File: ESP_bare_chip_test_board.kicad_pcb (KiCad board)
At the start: 4 copper layers, 57.1 x 63.5 mm, 92 parts, among them J1101 Conn_01x04, J1201 NorComp - 112-024-113RYY1, J1301 Conn_01x06, J1302 Conn_01x06, J1501 Conn_01x04, J1502 Conn_01x04, J201 Conn_01x06, J501 Barrel_Jack, J502 PWR_IN, J503 ALTERNATE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

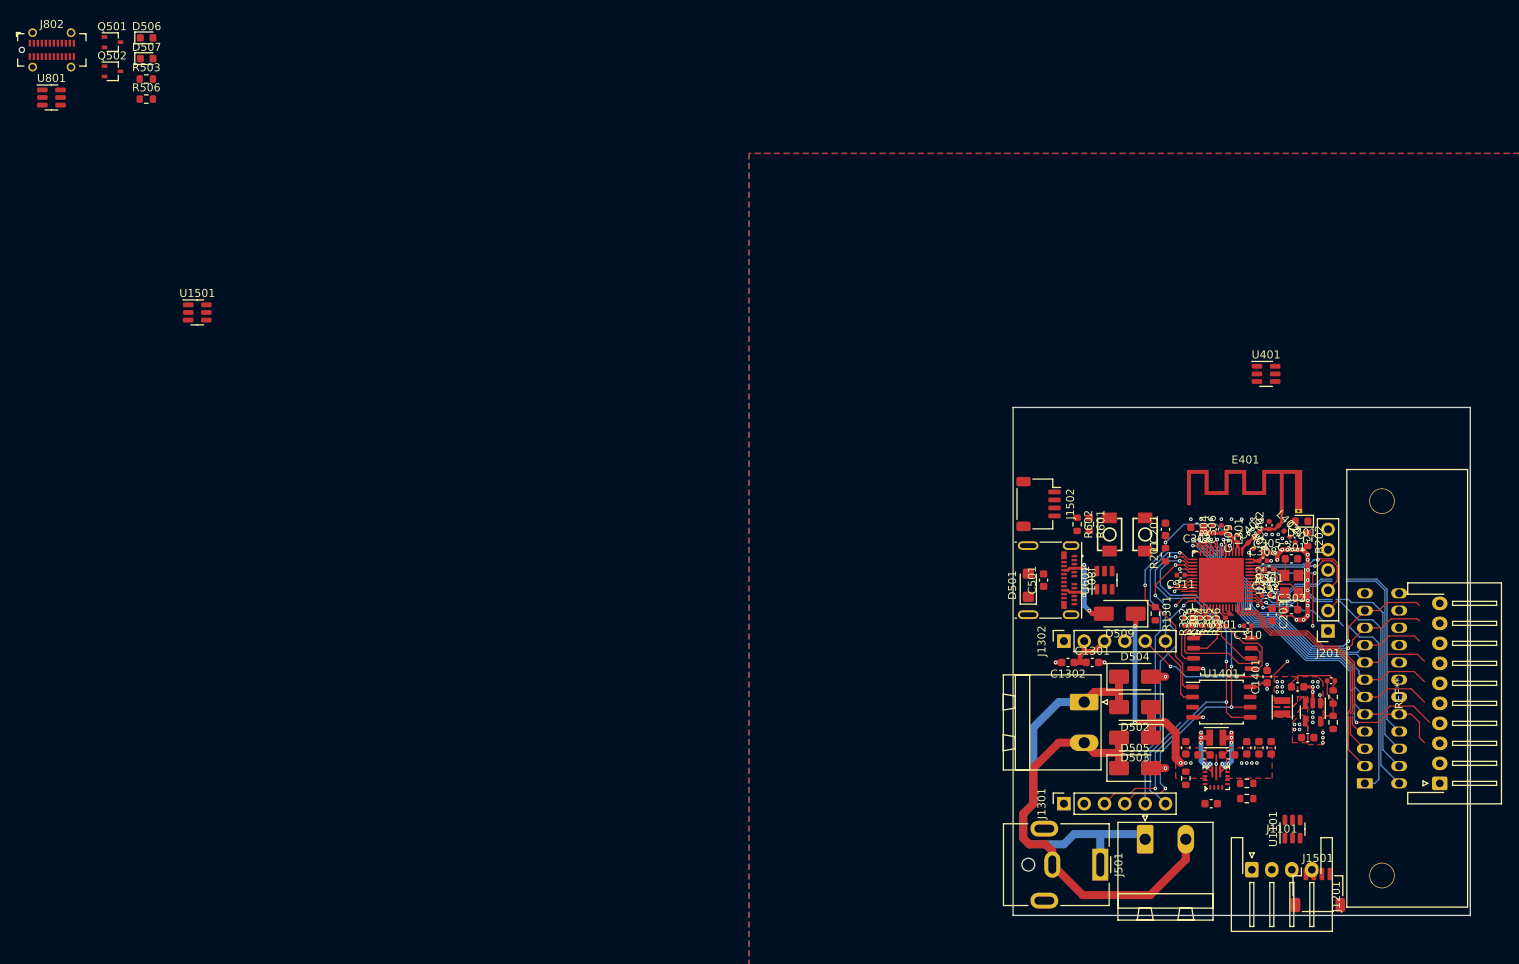
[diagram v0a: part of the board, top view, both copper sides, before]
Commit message: Position final few components
Removed one ESD diode arrray - experimental board, so not really needed,
with the exception of the USB lines.

Add and position 5V indicator LED

Finished wiring up the 5V buck-boost regulator
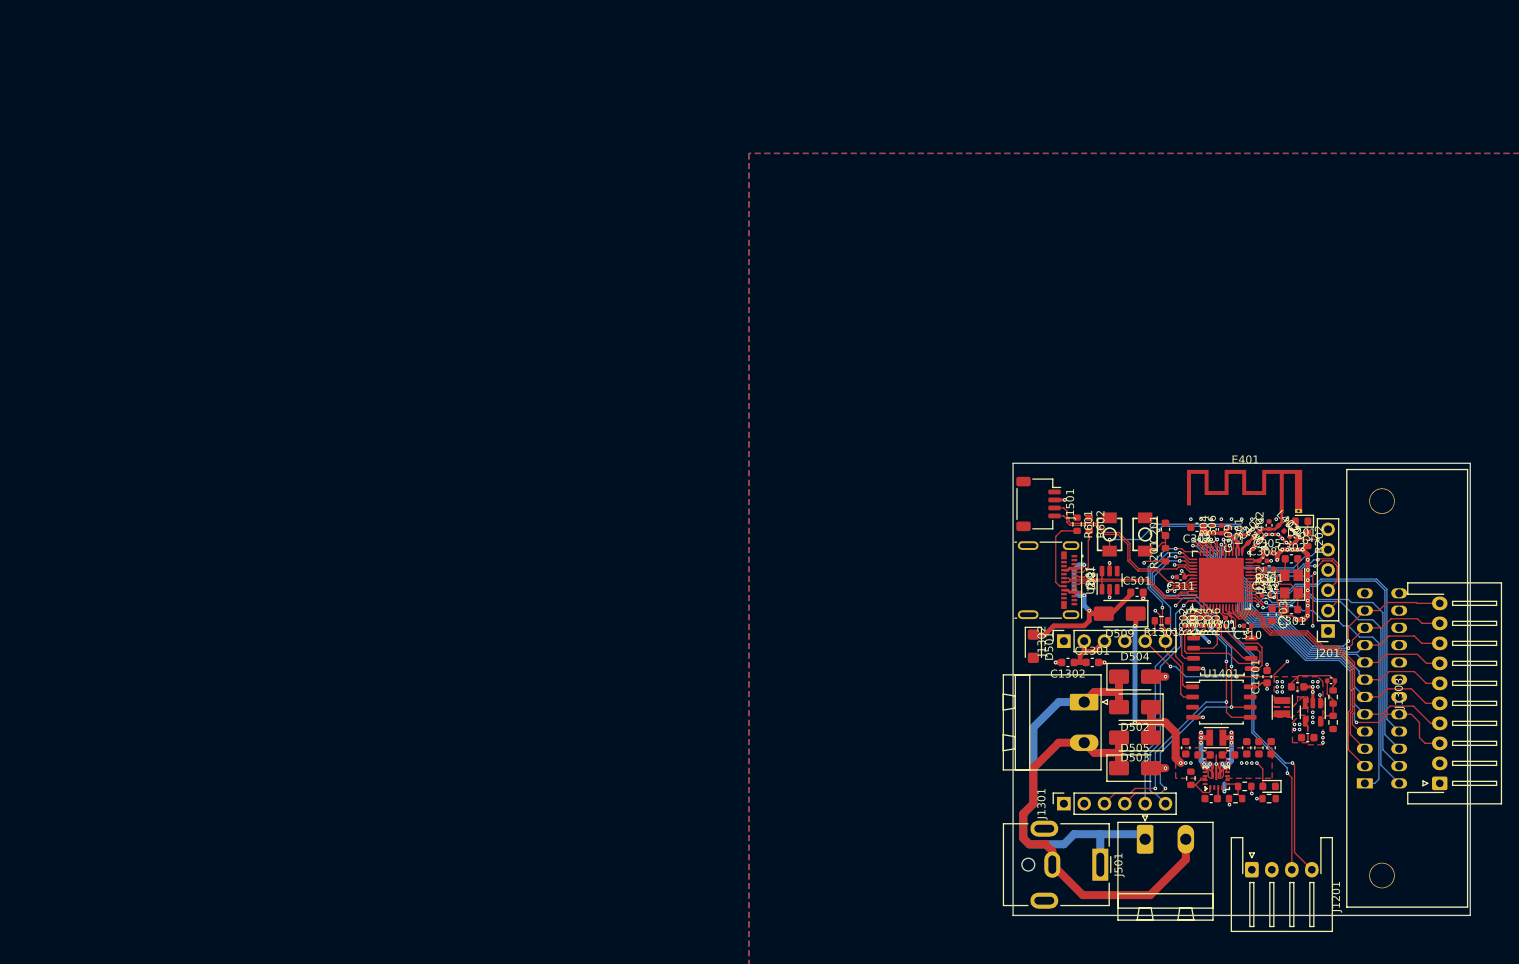
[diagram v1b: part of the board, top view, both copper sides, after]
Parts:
- removed D506: GREEN, LED_SMD:LED_0603_1608Metric
- removed J1502: Conn_01x04, Connector_JST:JST_SH_SM04B-SRSS-TB_1x04-1MP_P1.00mm_Horizontal
- removed J802: USB_C_Receptacle, Connector_USB:USB_C_Receptacle_GCT_USB4115-03-C
- removed Q501, Q502: DTC114E, Package_TO_SOT_SMD:SOT-323_SC-70
- removed R503: 100kΩ, Resistor_SMD:R_0603_1608Metric
- removed REF**: JST_XH_S10B-XH-A-1_1x10_P2.50mm_Horizontal, Connector_JST:JST_XH_S10B-XH-A-1_1x10_P2.50mm_Horizontal
- removed U1101, U1501, U601: D1213A-04TS-7, Package_TO_SOT_SMD:TSOT-23-6
- removed U401: MASWSS0179, Package_TO_SOT_SMD:SOT-23-6
- added J1303: Conn_01x10, Connector_JST:JST_XH_S10B-XH-A-1_1x10_P2.50mm_Horizontal, F.Cu at (167.6, 94.0)
- added NT901: NetTie_2, NetTie:NetTie-2_SMD_Pad0.5mm, B.Cu at (140.7, 94.5)
- moved D507 167.2 mm to (146.3, 94.4), turned to 180 degrees
- moved R506 165.4 mm to (146.3, 95.9), turned to 180 degrees
- moved U801 145.4 mm to (126.4, 68.6), turned to 90 degrees
- moved J1501 59.6 mm to (117.5, 59.1), turned to -90 degrees
- moved C501 11.8 mm to (129.8, 70.1), turned to 0 degrees
- moved D501 7.65 mm to (116.8, 76.8), turned to -90 degrees
- moved C301 6.35 mm to (149.1, 72.3), turned to 180 degrees
- moved C302 6.35 mm to (149.1, 65.9)
- moved R601 1.52 mm to (122.3, 61.6)
- moved R602 1.52 mm to (123.8, 61.6)
- moved R1005 1.40 mm to (142.1, 95.9)
- moved R1301 1.17 mm to (132.8, 73.7), turned to 180 degrees
- moved R1003 0.64 mm to (136.5, 93.3)
- moved C1012 0.63 mm to (139.1, 95.9)
- moved R1004 0.46 mm to (143.3, 94.4)
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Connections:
- J1101 pad 2: Net-(J1101-Pin_2) -> +5V
- J1201 pad 1: /ESP32-S3/IO42 -> /ESP32-S3/IO39
- J1201 pad 13: /ESP32-S3/IO38 -> /ESP32-S3/IO40
- J1201 pad 14: /ESP32-S3/IO37 -> /ESP32-S3/IO38
- J1201 pad 15: /ESP32-S3/IO36 -> /ESP32-S3/IO41
- J1201 pad 16: /ESP32-S3/IO35 -> /ESP32-S3/IO42
- J1201 pad 2: /ESP32-S3/IO41 -> /ESP32-S3/IO35
- J1201 pad 3: /ESP32-S3/IO40 -> /ESP32-S3/IO36
- J1201 pad 4: /ESP32-S3/IO39 -> /ESP32-S3/IO37
- J1501 pad 2: Net-(J1501-Pin_2) -> +3V3
- J1501 pad 3: /4pin_connector/J0_pin3 -> /ESP32-S3/IO14
- J1501 pad 4: /4pin_connector/J0_pin4 -> /ESP32-S3/IO15
- R506 pad 2: Net-(Q502-C) -> GND
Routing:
- net /4pin_connector/J0_pin4: track 1.29 -> 38.0 mm, vias 0 -> 2
- net /4pin_connector/J0_pin3: track 1.57 -> 36.9 mm, vias 0 -> 2
- net /ESP32-S3/ESP_EN: track 13.6 -> 38.9 mm, vias 2 -> 4
- net /ESP32-S3/IO37: track 50.6 -> 27.2 mm
- net /ESP32-S3/IO40: track 16.4 -> 39.4 mm
- net /ESP32-S3/ESP_BOOT: track 0.89 -> 22.7 mm, vias 1 -> 2
- net GND: track 36.5 -> 58.4 mm, vias 56 -> 71
- net /ESP32-S3/IO39: track 16.4 -> 37.8 mm
- net /USB_D-: track 1.51 -> 22.8 mm, vias 0 -> 2
- net /ESP32-S3/IO14: track 1.93 -> 22.7 mm, vias 1 -> 0
- net /ESP32-S3/IO36: track 50.0 -> 29.2 mm
- net /ESP32-S3/IO15: track 1.90 -> 22.6 mm, vias 1 -> 0
- net /ESP32-S3/IO41: track 18.9 -> 39.4 mm
- net /USB_D+: track 1.39 -> 21.5 mm, vias 0 -> 2
- net /ESP32-S3/IO35: track 48.2 -> 31.5 mm
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- added copper zone on F.Cu, net /Power/buck-boost-5v/L1
- added copper zone on F.Cu, net /Power/buck-boost-5v/L2
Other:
- board size 57.1 x 63.5 mm -> 57.1 x 56.5 mm

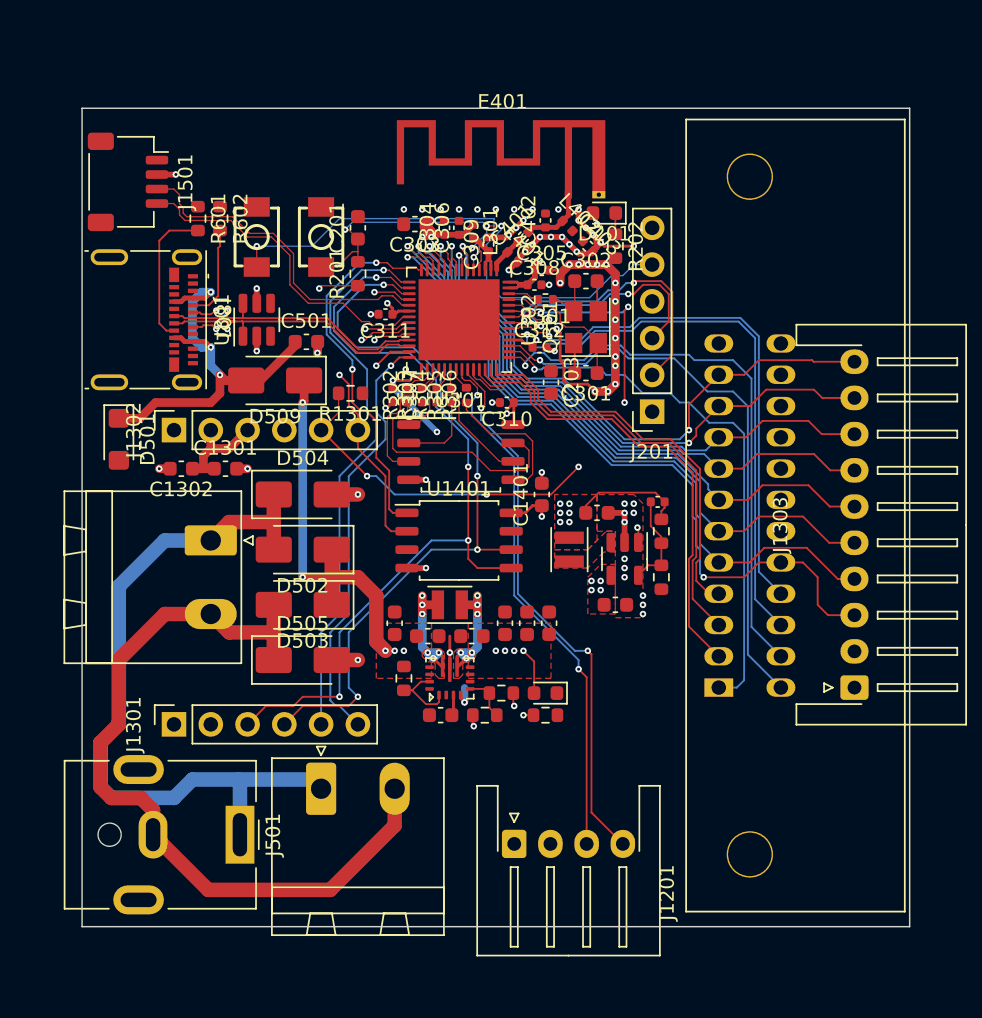
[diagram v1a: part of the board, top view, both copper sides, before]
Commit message: Wire remaining traces, fix DRC errors
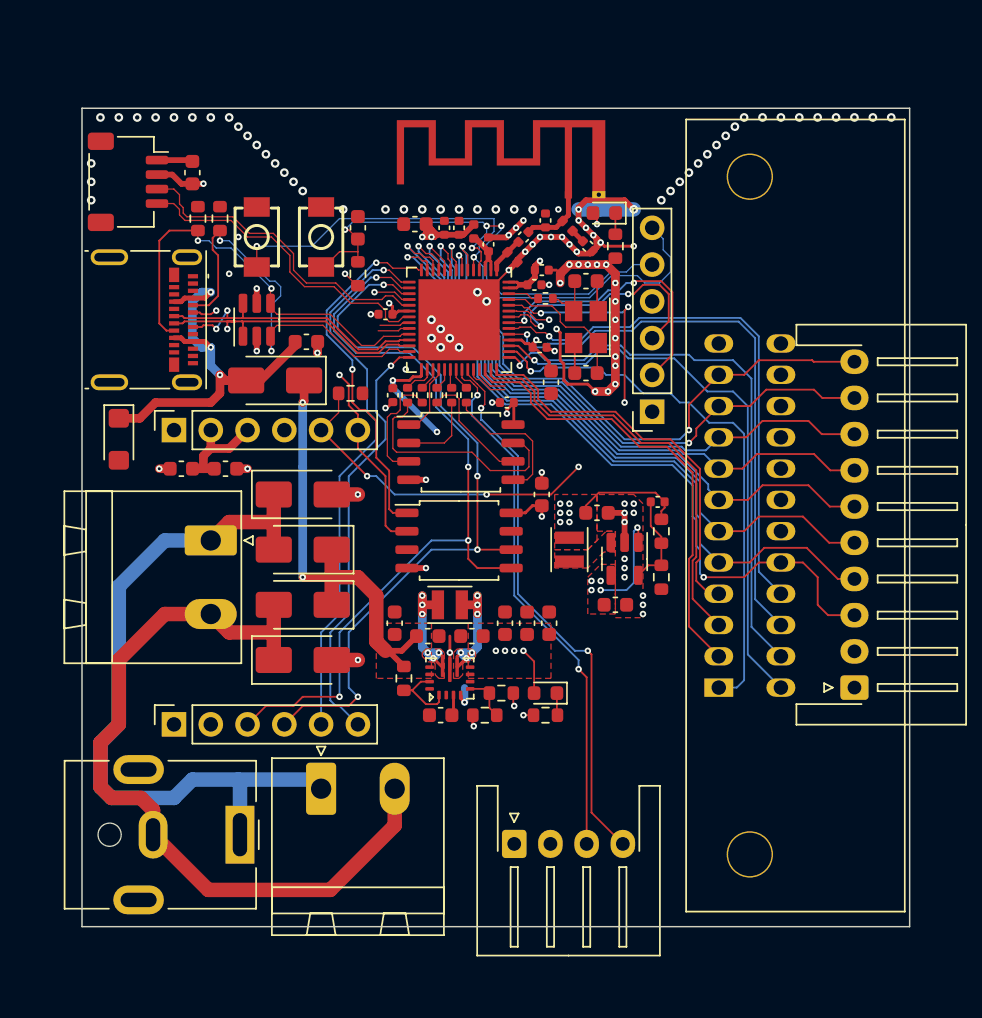
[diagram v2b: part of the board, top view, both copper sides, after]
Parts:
- added C1402: 22uF/6.3V, Capacitor_SMD:C_0603_1608Metric, F.Cu at (121.9, 58.4)
- moved R301 0.08 mm to (146.3, 67.1)
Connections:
- net I2C0.INT renamed /ESP32-S3/IO45
- net I2C0.SCL renamed /ESP32-S3/IO34
- net I2C0.SDA renamed /ESP32-S3/IO33
- U302 pad 24: /ESP32-S3/IO18 -> /USB/CC2
- U302 pad 27: /ESP32-S3/IO21 -> /USB/CC1
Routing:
- net /USB/CC1: track 6.57 -> 30.1 mm, vias 0 -> 2
- net GND: track 58.4 -> 79.0 mm, vias 71 -> 121
- net /ESP32-S3/ESP_BOOT: track 22.7 -> 42.8 mm
- net /USB/CC2: track 9.90 -> 29.4 mm, vias 0 -> 2
- net +5V: track 5.19 -> 11.6 mm
- net /Power/V_{IN}: track 27.1 -> 31.4 mm, vias 5 -> 2
- net +3V3: track 40.2 -> 43.0 mm
- net /ESP32-S3/IO21: track 2.68 -> 0.00 mm, vias 1 -> 0
- net /ESP32-S3/IO18: track 2.57 -> 0.00 mm, vias 1 -> 0
- net (no net): track 2.27 -> 0.00 mm
- net Net-(D507-K): track 0.00 -> 1.54 mm
- net /USB_D+: track 21.5 -> 23.0 mm
- net /ESP32-S3/IO17: track 3.62 -> 2.22 mm, vias 1 -> 0
- net /Power/buck-boost-5v/L2: track 10.4 -> 11.7 mm
- net /Power/buck-boost-5v/L1: track 9.03 -> 10.3 mm
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
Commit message: Add test pads for extra IO pins
Can be soldered to if desired for some testing purpose
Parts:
- added TP101: TestPoint, TestPoint:TestPoint_Pad_D2.0mm, F.Cu at (147.3, 77.5)
- added TP102: TestPoint, TestPoint:TestPoint_Pad_D2.0mm, F.Cu at (151.1, 78.7)
- added TP103: TestPoint, TestPoint:TestPoint_Pad_D2.0mm, F.Cu at (158.1, 66.0)
- added TP104: TestPoint, TestPoint:TestPoint_Pad_D2.0mm, F.Cu at (152.4, 99.1)
- added TP105: TestPoint, TestPoint:TestPoint_Pad_D2.0mm, F.Cu at (146.1, 99.1)
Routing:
- net /ESP32-S3/IO17: track 2.22 -> 70.5 mm, vias 0 -> 4
- net /ESP32-S3/IO16: track 2.10 -> 58.9 mm, vias 0 -> 2
- net /ESP32-S3/IO45: track 3.03 -> 16.2 mm, vias 1 -> 3
- net /ESP32-S3/IO34: track 2.46 -> 12.8 mm
- net /ESP32-S3/IO33: track 3.03 -> 9.64 mm
- net /ESP32-S3/IO41: track 39.4 -> 40.9 mm
- net /ESP32-S3/IO40: track 39.4 -> 40.3 mm
- net GND: vias 121 -> 122

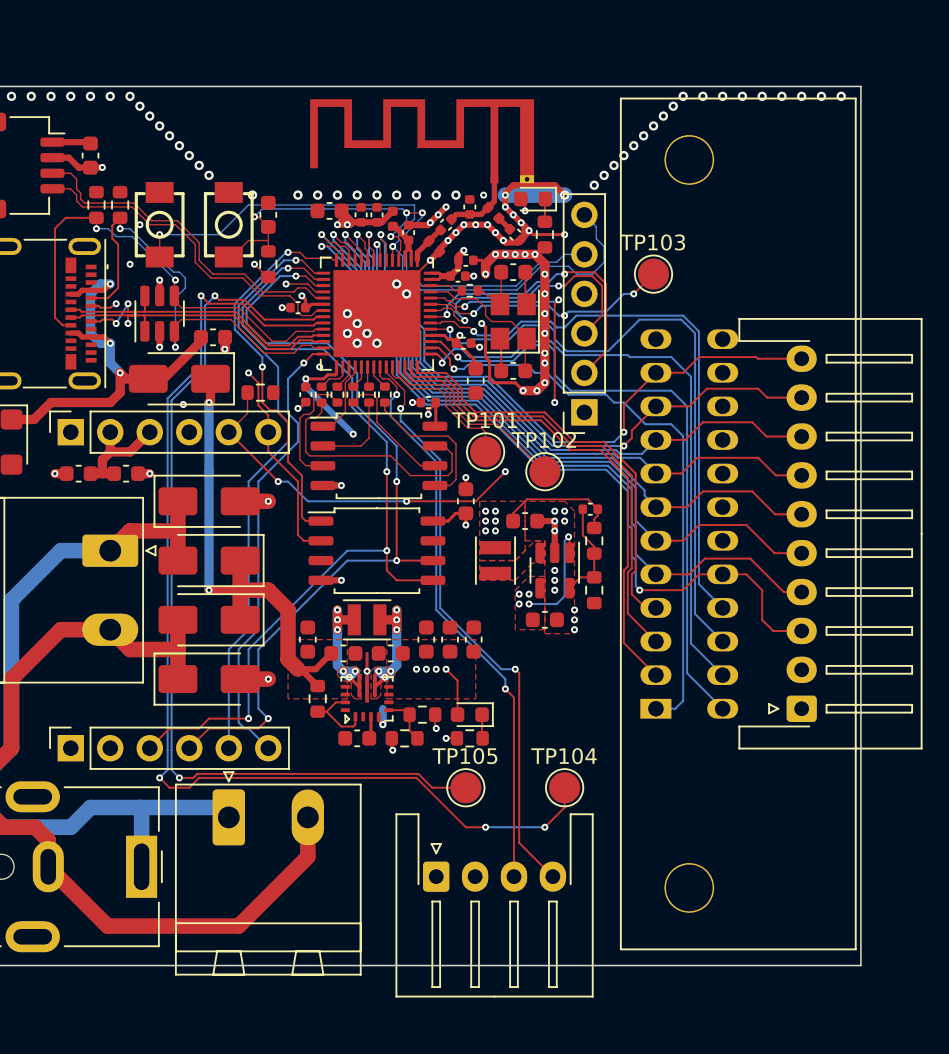
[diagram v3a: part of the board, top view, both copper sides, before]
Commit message: Free up IO26 (to allow for PSRAM)
Had spare IO lines, so may as well use a different one to do ETH_INT
instead of IO26.
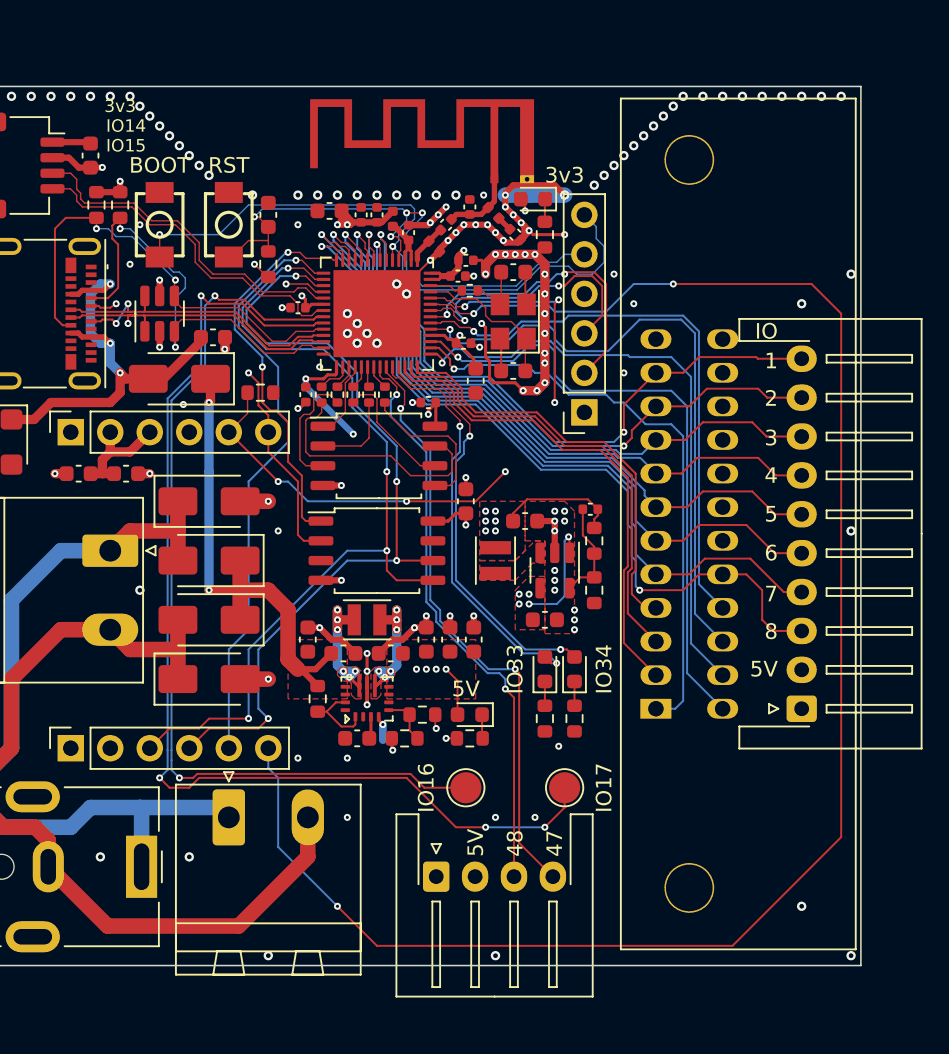
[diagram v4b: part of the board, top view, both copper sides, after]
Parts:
- removed TP101, TP102, TP103: TestPoint, TestPoint:TestPoint_Pad_D2.0mm
- added D101: YELLOW, LED_SMD:LED_0603_1608Metric, F.Cu at (151.1, 91.4)
- added D102: YELLOW, LED_SMD:LED_0603_1608Metric, F.Cu at (153.0, 91.4)
- added R101: 10kΩ, Resistor_SMD:R_0603_1608Metric, F.Cu at (151.1, 94.6)
- added R102: 10kΩ, Resistor_SMD:R_0603_1608Metric, F.Cu at (153.0, 94.6)
- moved NT901 1.00 mm to (140.7, 95.5), turned to -90 degrees
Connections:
- net /4pin_connector/J0_pin3 renamed /IO48
- net /4pin_connector/J0_pin4 renamed /IO47
- U302 pad 28: /~{ETH_INT} -> /ESP32-S3/IO26
- U302 pad 51: /ESP32-S3/IO45 -> /~{ETH_INT}
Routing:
- net /~{ETH_INT}: track 29.5 -> 110.5 mm, vias 1 -> 3
- net /ESP32-S3/IO33: track 9.64 -> 26.8 mm, vias 0 -> 2
- net /ESP32-S3/IO45: track 16.2 -> 0.00 mm, vias 3 -> 0
- net /ESP32-S3/IO34: track 12.8 -> 26.7 mm, vias 0 -> 2
- net GND: track 79.0 -> 91.0 mm, vias 122 -> 151
- net Net-(D102-K): track 0.00 -> 1.56 mm
- net Net-(D101-K): track 0.00 -> 1.56 mm
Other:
- board text added: "1"
- board text added: "2"
- board text added: "3"
- board text added: "3v3"
- board text added: "4"
- board text added: "47"
- board text added: "48"
- board text added: "5"
- board text added: "5V"
- board text added: "6"
- board text added: "7"
- board text added: "8"
- board text added: "BOOT"
- board text added: "IO"
- board text added: "IO14"
- board text added: "IO15"
- board text added: "IO16"
- board text added: "IO17"
- board text added: "IO33"
- board text added: "IO34"
- board text added: "RST"
